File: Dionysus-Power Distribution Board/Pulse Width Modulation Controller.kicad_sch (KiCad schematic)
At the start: 14 parts

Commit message: Added Libraries and Copied previous work
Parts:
- removed C? (x2): C, symbol Device:C
- removed H? (x2): TLC59711PWPR, SOP65P640X120-21N, symbol Power Distribution Board-rescue:TLC59711PWPR-Driver_LED
- removed J?: LED CH3, TerminalBlock_Phoenix:TerminalBlock_Phoenix_MKDS-1,5-3_1x03_P5.00mm_Horizontal, symbol Connector:Screw_Terminal_01x03
- removed J?: LED CH8, TerminalBlock_Phoenix:TerminalBlock_Phoenix_MKDS-1,5-3_1x03_P5.00mm_Horizontal, symbol Connector:Screw_Terminal_01x03
- removed J?: LED CH4, TerminalBlock_Phoenix:TerminalBlock_Phoenix_MKDS-1,5-3_1x03_P5.00mm_Horizontal, symbol Connector:Screw_Terminal_01x03
- removed J?: LED CH1, TerminalBlock_Phoenix:TerminalBlock_Phoenix_MKDS-1,5-3_1x03_P5.00mm_Horizontal, symbol Connector:Screw_Terminal_01x03
- removed J?: LED CH2, TerminalBlock_Phoenix:TerminalBlock_Phoenix_MKDS-1,5-3_1x03_P5.00mm_Horizontal, symbol Connector:Screw_Terminal_01x03
- removed J?: LED CH6, TerminalBlock_Phoenix:TerminalBlock_Phoenix_MKDS-1,5-3_1x03_P5.00mm_Horizontal, symbol Connector:Screw_Terminal_01x03
- removed J?: LED CH7, TerminalBlock_Phoenix:TerminalBlock_Phoenix_MKDS-1,5-3_1x03_P5.00mm_Horizontal, symbol Connector:Screw_Terminal_01x03
- removed J?: LED CH5, TerminalBlock_Phoenix:TerminalBlock_Phoenix_MKDS-1,5-3_1x03_P5.00mm_Horizontal, symbol Connector:Screw_Terminal_01x03
- removed R? (x2): R_US, symbol Device:R_US
- added C? (x2): C, symbol Device:C
- added H? (x2): TLC59711PWPR, SOP65P640X120-21N, symbol Power Distribution Board-rescue:TLC59711PWPR-Driver_LED
- added J?: LED CH1, TerminalBlock_Phoenix:TerminalBlock_Phoenix_MKDS-1,5-3_1x03_P5.00mm_Horizontal, symbol Connector:Screw_Terminal_01x03
- added J?: LED CH3, TerminalBlock_Phoenix:TerminalBlock_Phoenix_MKDS-1,5-3_1x03_P5.00mm_Horizontal, symbol Connector:Screw_Terminal_01x03
- added J?: LED CH5, TerminalBlock_Phoenix:TerminalBlock_Phoenix_MKDS-1,5-3_1x03_P5.00mm_Horizontal, symbol Connector:Screw_Terminal_01x03
- added J?: LED CH7, TerminalBlock_Phoenix:TerminalBlock_Phoenix_MKDS-1,5-3_1x03_P5.00mm_Horizontal, symbol Connector:Screw_Terminal_01x03
- added J?: LED CH8, TerminalBlock_Phoenix:TerminalBlock_Phoenix_MKDS-1,5-3_1x03_P5.00mm_Horizontal, symbol Connector:Screw_Terminal_01x03
- added J?: LED CH4, TerminalBlock_Phoenix:TerminalBlock_Phoenix_MKDS-1,5-3_1x03_P5.00mm_Horizontal, symbol Connector:Screw_Terminal_01x03
- added J?: LED CH2, TerminalBlock_Phoenix:TerminalBlock_Phoenix_MKDS-1,5-3_1x03_P5.00mm_Horizontal, symbol Connector:Screw_Terminal_01x03
- added J?: LED CH6, TerminalBlock_Phoenix:TerminalBlock_Phoenix_MKDS-1,5-3_1x03_P5.00mm_Horizontal, symbol Connector:Screw_Terminal_01x03
- added R? (x2): R_US, symbol Device:R_US
- added U? (x2): TLC59711PWPR, SOP65P640X120-21N, symbol Driver_LED_jal:TLC59711PWPR
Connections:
- net CH1-B: now also H?.5 (OUTB0), J?.1 (Pin_1)
- net CH1-G: now also H?.4 (OUTG0), J?.2 (Pin_2)
- net CH1-R: now also H?.3 (OUTR0), J?.3 (Pin_3)
- net CH2-B: now also H?.8 (OUTB1), J?.1 (Pin_1)
- net CH2-G: now also H?.7 (OUTG1), J?.2 (Pin_2)
- net CH2-R: now also H?.6 (OUTR1), J?.3 (Pin_3)
- net CH3-B: now also H?.16 (OUTR3), J?.3 (Pin_3)
- net CH3-G: now also H?.17 (OUTG3), J?.2 (Pin_2)
- net CH3-R: now also H?.18 (OUTB3), J?.1 (Pin_1)
- net CH4-B: now also H?.13 (OUTR2), J?.3 (Pin_3)
- net CH4-G: now also H?.14 (OUTG2), J?.2 (Pin_2)
- net CH4-R: now also H?.15 (OUTB2), J?.1 (Pin_1)
- net CH5-B: now also H?.5 (OUTB0), J?.1 (Pin_1)
- net CH5-G: now also H?.4 (OUTG0), J?.2 (Pin_2)
- net CH5-R: now also H?.3 (OUTR0), J?.3 (Pin_3)
- net CH6-B: now also H?.8 (OUTB1), J?.1 (Pin_1)
- net CH6-G: now also H?.7 (OUTG1), J?.2 (Pin_2)
- net CH6-R: now also H?.6 (OUTR1), J?.3 (Pin_3)
- net CH7-B: now also H?.16 (OUTR3), J?.3 (Pin_3)
- net CH7-G: now also H?.17 (OUTG3), J?.2 (Pin_2)
- net CH7-R: now also H?.18 (OUTB3), J?.1 (Pin_1)
- net CH8-B: now also H?.13 (OUTR2), J?.3 (Pin_3)
- net CH8-G: now also H?.14 (OUTG2), J?.2 (Pin_2)
- net CH8-R: now also H?.15 (OUTB2), J?.1 (Pin_1)
- net GND: now also C?.2, C?.2, H?.2 (GND), H?.2 (GND), H?.21 (PAD), H?.21 (PAD), R?.2, R?.2
- net PDB_PWR3: now also H?.19 (VCC), H?.19 (VCC)
- net TWCK0: now also H?.10 (SCKI)
- net TWD0: now also H?.9 (SDTI)
- net VREG0: now also C?.1, H?.20 (VREG)
- net VREG1: now also C?.1, H?.20 (VREG)
- new net: H?.1 (IREF), R?.1 (x2)
- new net: H?.10 (SCKI), H?.11 (SCKO)
- new net: H?.12 (SDTO), H?.9 (SDTI)
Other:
- note removed: "Adafruit 12-channel 16-bit PWM LED driver - SPI interface - TLC59711 (ID: 1455) TI TLC59711 PWM RGB LED Driver"
- note removed: "TLC59711PWPR internal linear voltage regulator operates from 4.0V to 17.0V NEED A SEPARATE REGULATED SUPPLY FOR PWM CONTROLLER"
- title: Power Distribution Board, Dionysus -> (none)

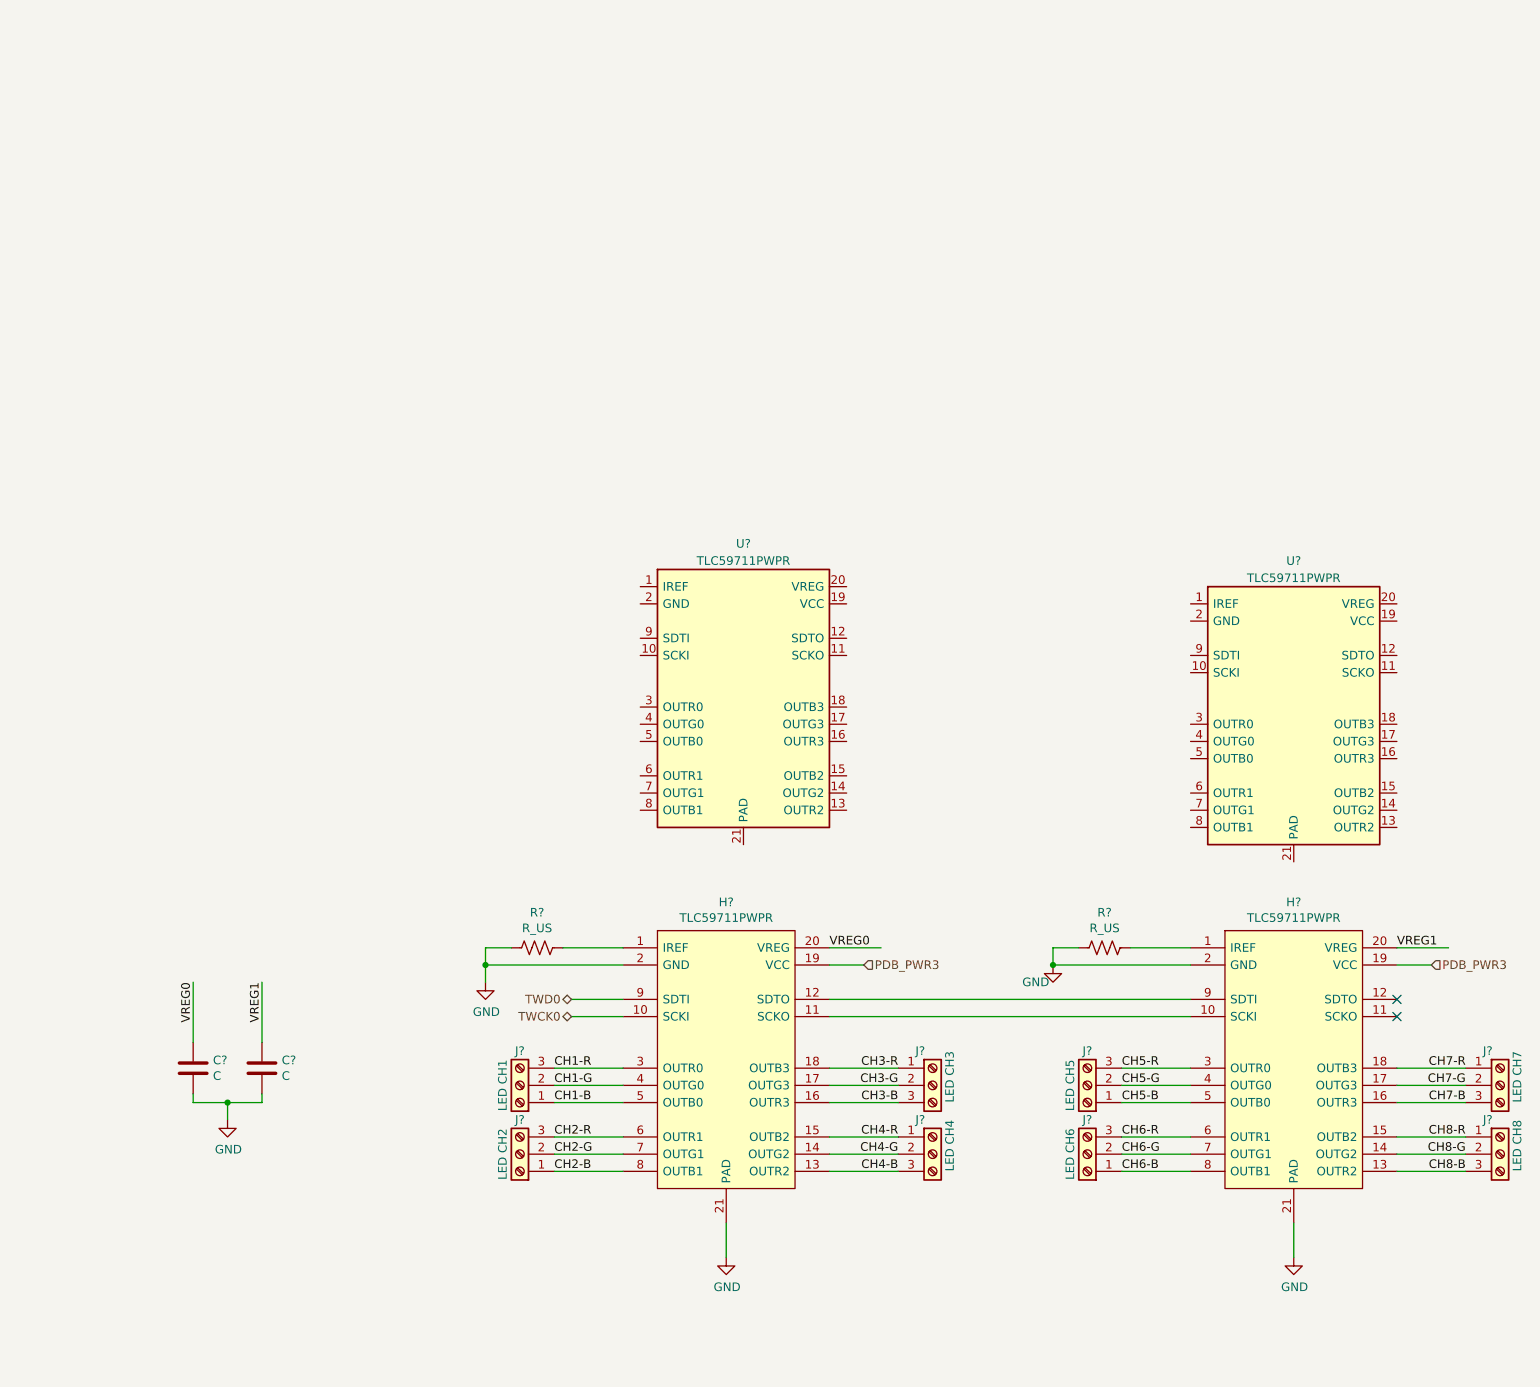
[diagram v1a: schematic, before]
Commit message: Updated Symbols and Redefined Hierarchical Pins
Updated high side driver symbols, and added hierarchical pins to page 1
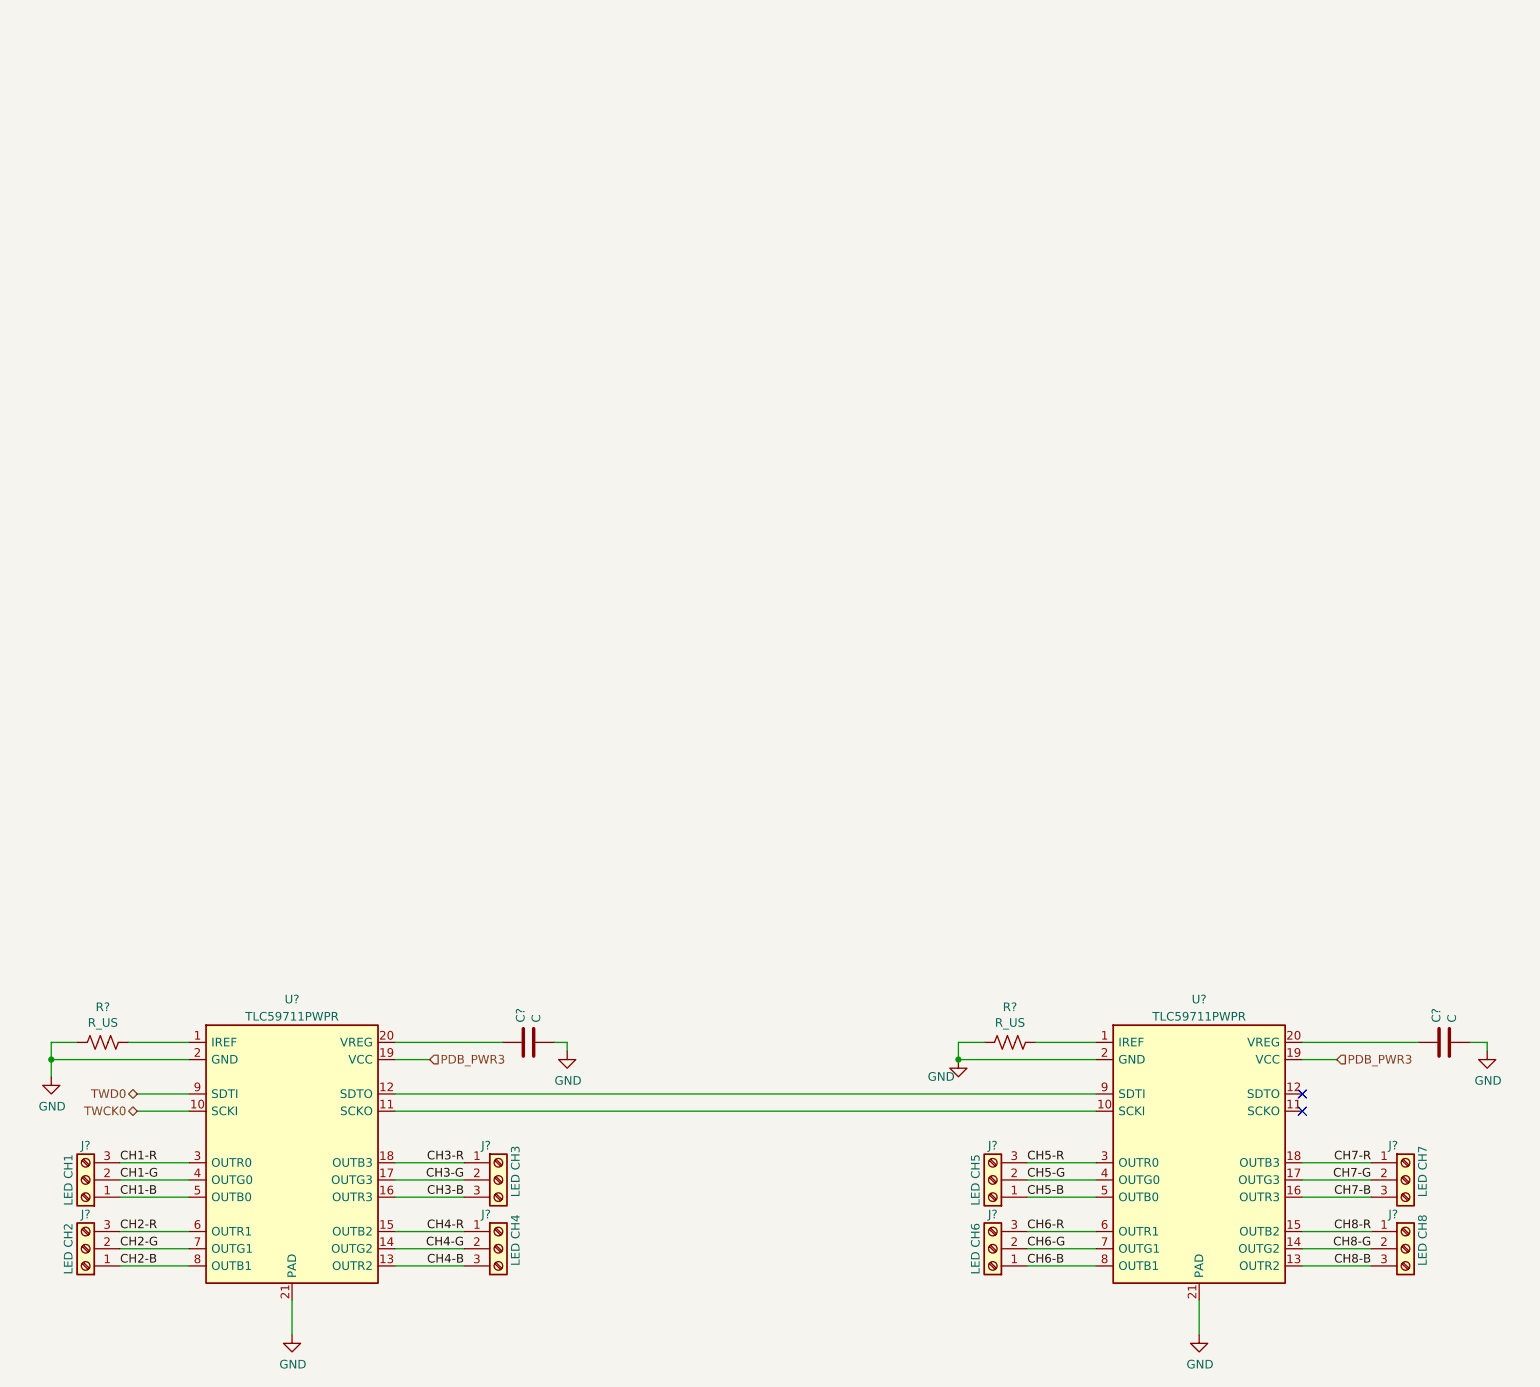
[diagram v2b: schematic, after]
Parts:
- removed H? (x2): TLC59711PWPR, SOP65P640X120-21N, symbol Power Distribution Board-rescue:TLC59711PWPR-Driver_LED
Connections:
- net VREG0 is gone; now on an unnamed net: C?.1
- net VREG1 is gone; now on an unnamed net: C?.1
- net CH1-B: now also U?.5 (OUTB0)
- net CH1-G: now also U?.4 (OUTG0)
- net CH1-R: now also U?.3 (OUTR0)
- net CH2-B: now also U?.8 (OUTB1)
- net CH2-G: now also U?.7 (OUTG1)
- net CH2-R: now also U?.6 (OUTR1)
- net CH3-B: now also U?.16 (OUTR3)
- net CH3-G: now also U?.17 (OUTG3)
- net CH3-R: now also U?.18 (OUTB3)
- net CH4-B: now also U?.13 (OUTR2)
- net CH4-G: now also U?.14 (OUTG2)
- net CH4-R: now also U?.15 (OUTB2)
- net CH5-B: now also U?.5 (OUTB0)
- net CH5-G: now also U?.4 (OUTG0)
- net CH5-R: now also U?.3 (OUTR0)
- net CH6-B: now also U?.8 (OUTB1)
- net CH6-G: now also U?.7 (OUTG1)
- net CH6-R: now also U?.6 (OUTR1)
- net CH7-B: now also U?.16 (OUTR3)
- net CH7-G: now also U?.17 (OUTG3)
- net CH7-R: now also U?.18 (OUTB3)
- net CH8-B: now also U?.13 (OUTR2)
- net CH8-G: now also U?.14 (OUTG2)
- net CH8-R: now also U?.15 (OUTB2)
- net GND: now also U?.2 (GND), U?.2 (GND), U?.21 (PAD), U?.21 (PAD)
- net PDB_PWR3: now also U?.19 (VCC), U?.19 (VCC)
- net TWCK0: now also U?.10 (SCKI)
- net TWD0: now also U?.9 (SDTI)
- net at R?.1: now also U?.1 (IREF)
- net at U?.10 (SCKI): now also U?.11 (SCKO)
- net at U?.9 (SDTI): now also U?.12 (SDTO)
- net at U?.1 (IREF): now also R?.1
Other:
- moved on the sheet: C?, J?, R?, U?
